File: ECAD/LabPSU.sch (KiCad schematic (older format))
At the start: 45 parts, among them J1 PWR

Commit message: how do i do this
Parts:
- removed U?: LM5118MH, Package_SO:Texas_PWP0020A, symbol Regulator_Switching:LM5118MH
- removed U?: MAX5035EUSA, Package_SO:SOIC-8_3.9x4.9mm_P1.27mm, symbol Regulator_Switching:MAX5035EUSA
- removed U?: INA285, symbol Amplifier_Current:INA285
- added C? (x3): 220uF, symbol Device:CP
- added D? (x2): 1N4148, symbol Device:D
- added R?: 10K, symbol Device:R
- added U? (x3): LM358, symbol Amplifier_Operational:LM358
- added U?: LM5118MH, Package_SO:Texas_PWP0020A, symbol Regulator_Switching:LM5118MH
- added U?: INA285, symbol Amplifier_Current:INA285
- added U?: MAX5035EUSA, Package_SO:SOIC-8_3.9x4.9mm_P1.27mm, symbol Regulator_Switching:MAX5035EUSA
- C? (x2): value C -> 47uF
- C? (x2): value C -> 1uF
- L?: value 300uH -> 470uH
- RV2: value 100K -> 160K
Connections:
- net +10V: now also U?.6 (V+), U?.8 (V+)
- net GND: now also C?.2, C?.2, C?.2, R?.2, U?.13 (CSG), U?.14 (PGND), U?.17 (VCCX), U?.2 (GND), U?.21 (EP), U?.3 (REF2), U?.3 (SGND), U?.4 (V-), U?.6 (AGND), U?.6 (GND), U?.7 (REF1)
- net VBUS: now also U?.1 (VIN), U?.7 (VIN)
- net VOUT: now also U?.1 (-), U?.10 (VOUT)
- net at D?.2 (A), R?.1: now also U?.12 (CS)
- net at Q?.4 (G): now also U?.15 (LO)
- net at C?.1: now also U?.16 (VCC)
- net at C?.1: now also U?.18 (HB)
- net at Q?.4 (G): now also U?.19 (HO)
- net at C?.2, D?.1 (K), L?.1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: now also U?.20 (HS)
- net at R?.1: now also U?.3 (RT)
- net at R?.2: now also U?.4 (EN)
- net at C?.1: now also U?.5 (RAMP)
- net at C?.1: now also U?.7 (SS)
- net FB: now reaches C?.1, R?.2
- net FB: now also D?.1 (K), D?.1 (K), R?.1, U?.2 (-), U?.6 (-), U?.8 (FB)
- net at C?.2, C?.2: now also U?.9 (COMP)
- net at C?.1: now also U?.1 (BST)
- net at C?.1: now also U?.2 (VD)
- net at R?.1, R?.2: now also U?.4 (FB)
- net at R?.1, R?.2: now also U?.5 (ON/~OFF~)
- net at C?.2, D?.1 (K), L?.1: now also U?.8 (LX)
- net at C?.1, C?.1, C?.1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: now also C?.1, C?.1, C?.1, U?.8 (+)
- net at R?.1, RV1.2, RV1.3: now also U?.5 (+)
- net at RV2.1: now also U?.5
- net at R?.1, RV2.2, RV2.3: now also U?.3 (+)
- new net: D?.2 (A), U?.1
- new net: D?.2 (A), U?.7
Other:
- note added: "Rtop/Rbottom = 1000*0.01Ohm*Iout/1.23V - 1\nAdjustable 0.123A to 1A"
- note added: "issue: output cant swing to 100V"
- note removed: "Rtop/Rbottom = 1000*0.01Ohm*Iout/1.23V - 1\nAdjustable 0.123A to 10A"
- moved on the sheet: C?, D?, J1, L?, Q?, R?, RV1A, RV1B, RV2A, RV2B

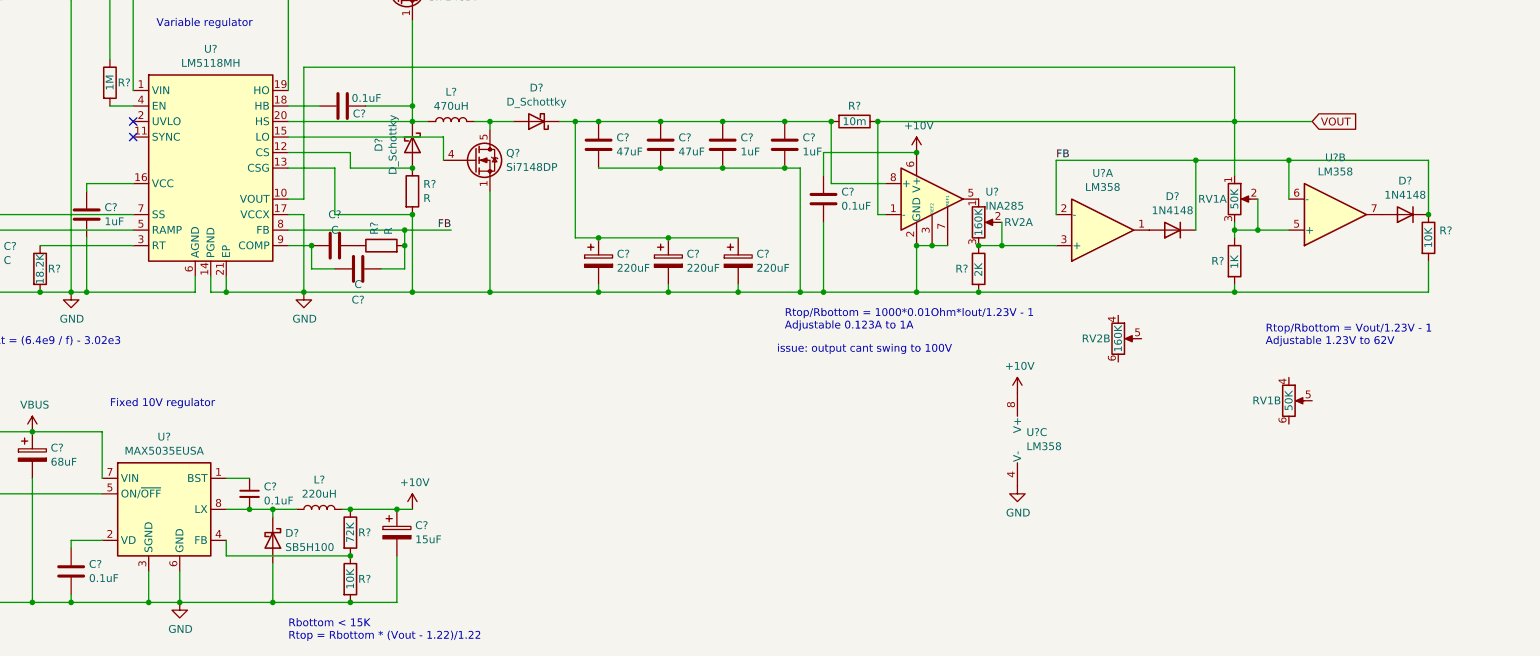
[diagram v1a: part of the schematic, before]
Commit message: vref for current sense
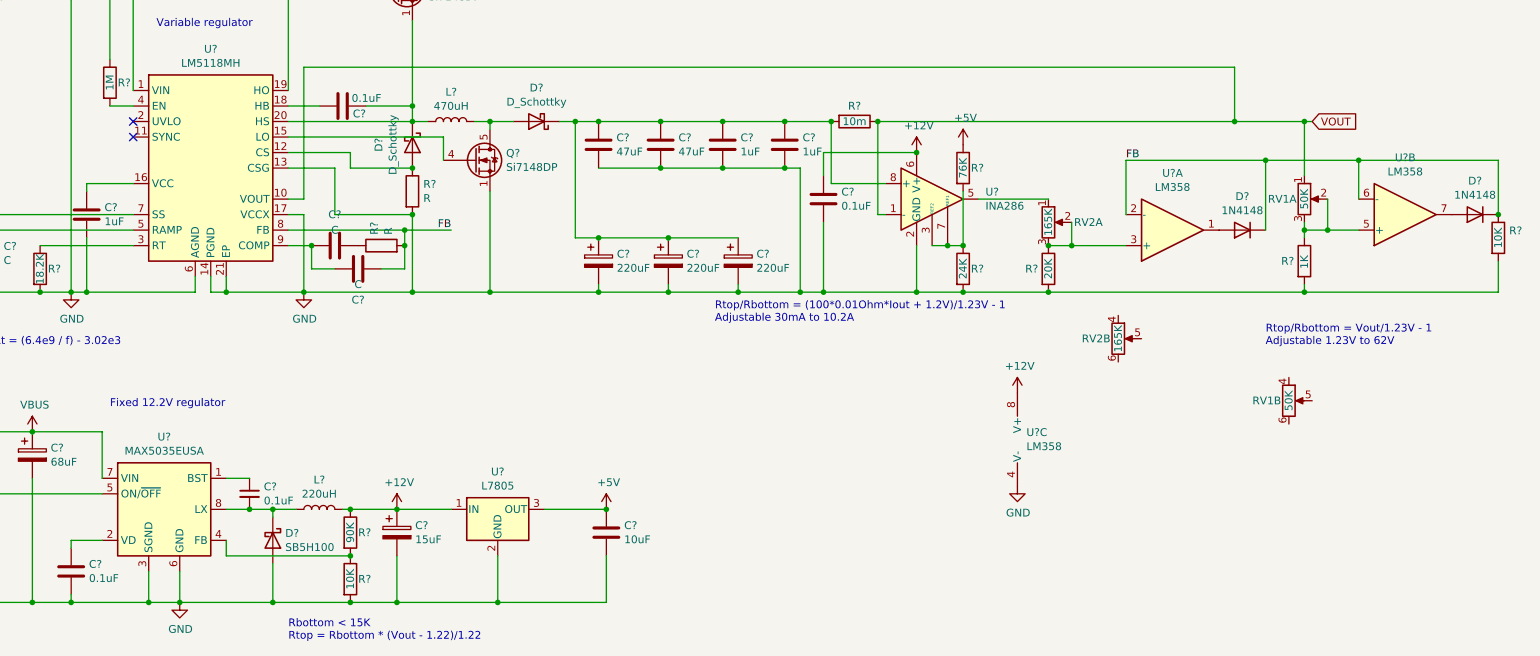
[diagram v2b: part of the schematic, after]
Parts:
- removed U?: INA285, symbol Amplifier_Current:INA285
- added C?: 10uF, symbol Device:C
- added R?: 24K, symbol Device:R
- added R?: 76K, symbol Device:R
- added U?: L7805, symbol Regulator_Linear:L7805
- added U?: INA286, symbol Amplifier_Current:INA286
- R?: value 72K -> 90K
- R?: value 2K -> 20K
- RV2: value 160K -> 165K
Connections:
- net GND: now also C?.2, R?.2, U?.2 (GND), U?.2 (GND)
- net VOUT: now also U?.1 (-)
- net at C?.1, C?.1, C?.1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: now also U?.8 (+)
- net at RV2.1: now also U?.5
- net +10V renamed +12V
- net +12V: now also U?.1 (IN), U?.6 (V+)
- new net: R?.1, R?.2, U?.3 (REF2), U?.7 (REF1)
- new net +5V: C?.1, R?.1, U?.3 (OUT)
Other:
- note added: "Fixed 12.2V regulator"
- note added: "Rtop/Rbottom = (100*0.01Ohm*Iout + 1.2V)/1.23V - 1\nAdjustable 30mA to 10.2A"
- note removed: "Fixed 10V regulator"
- note removed: "Rtop/Rbottom = 1000*0.01Ohm*Iout/1.23V - 1\nAdjustable 0.123A to 1A"
- note removed: "issue: output cant swing to 100V"
- moved on the sheet: D?, R?, RV1A, RV2A, U?A, U?B

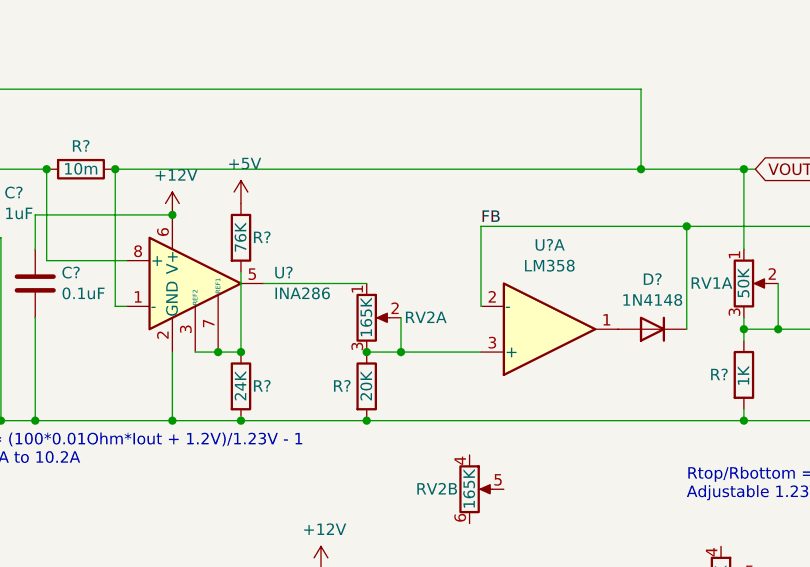
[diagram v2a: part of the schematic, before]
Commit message: add iout label
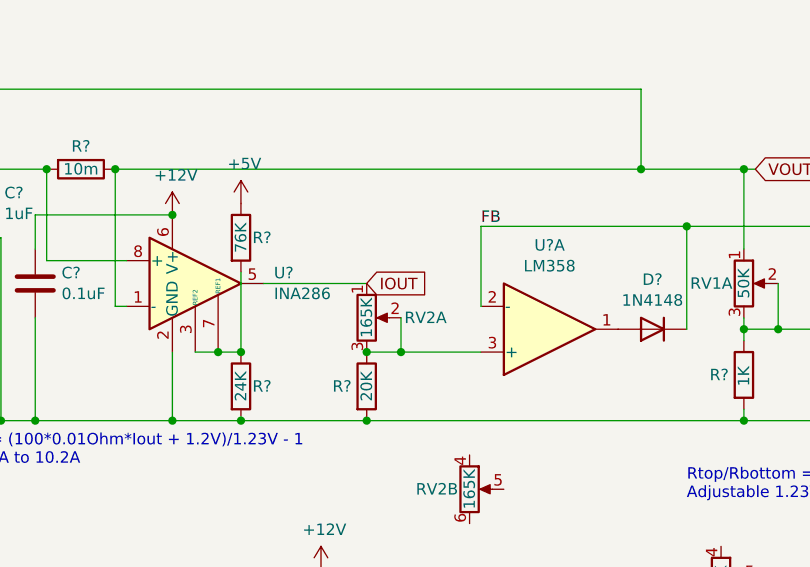
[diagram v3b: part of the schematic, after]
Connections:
- net IOUT: now reaches RV2.1, U?.5
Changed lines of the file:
@@
 $EndComp
 Connection ~ 8500 3000
+Text GLabel 9350 3300 2    50   Input ~ 0
+IOUT
 $EndSCHEMATC

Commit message: add load circuit
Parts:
- added Q?: IRLZ44N, Package_TO_SOT_THT:TO-220-3_Vertical, symbol Transistor_FET:IRLZ44N
- added R? (x10): 10R, symbol Device:R
- added R?: 10m, symbol Device:R
- added R?: 50R, symbol Device:R
- added R?: 1.5K, symbol Device:R
- added RV3: 50K, symbol Device:R_POT_Dual_Separate
- added U2: LM358, symbol Amplifier_Operational:LM358
- added U?: LT6106, Package_TO_SOT_SMD:SOT-23-5, symbol Amplifier_Current:LT6106
- gave numbers to parts that had none: 1
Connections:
- net +12V: now also RV3.1, U2.8 (V+)
- net GND: now also RV3.3, U2.4 (V-), U2.5 (+)
- new net: Q?.1 (G), U2.1
- new net: Q?.3 (S), R?.1, R?.1, R?.1, R?.1, R?.1, R?.1, R?.1, R?.1, R?.1, R?.1, U2.2 (-)
- new net: RV3.2, U2.3 (+)
- new net: U2.6 (-), U2.7
- new net: Q?.2 (D), R?.2, U?.4 (+)
- new net: R?.1, U?.3 (-)
- new net ILOAD: R?.2, U?.1
- new net VLOAD+: R?.1, R?.2, U?.5 (V+)
- new net VLOAD-: R?.1, R?.2, R?.2, R?.2, R?.2, R?.2, R?.2, R?.2, R?.2, R?.2, R?.2, U?.2 (V-)

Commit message: downscale
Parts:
- removed C?: 68uF, symbol Device:CP
- removed C?: 0.1uF, symbol Device:C
- removed C?: 0.1uF, symbol Device:C_Small
- removed C?: 15uF, symbol Device:CP
- removed D?: SB5H100, symbol Device:D_Schottky
- removed L?: 220uH, symbol Device:L
- removed Q?: IRLZ44N, Package_TO_SOT_THT:TO-220-3_Vertical, symbol Transistor_FET:IRLZ44N
- removed R?: 150K, symbol Device:R
- removed R?: 1M, symbol Device:R
- removed R?: 90K, symbol Device:R
- removed R?: 10K, symbol Device:R
- removed R? (x10): 10R, symbol Device:R
- removed R?: 10m, symbol Device:R
- removed R?: 50R, symbol Device:R
- removed R?: 1.5K, symbol Device:R
- removed RV3: 50K, symbol Device:R_POT_Dual_Separate
- removed U2: LM358, symbol Amplifier_Operational:LM358
- removed U?: L7805, symbol Regulator_Linear:L7805
- removed U?: MAX5035EUSA, Package_SO:SOIC-8_3.9x4.9mm_P1.27mm, symbol Regulator_Switching:MAX5035EUSA
- removed U?: LT6106, Package_TO_SOT_SMD:SOT-23-5, symbol Amplifier_Current:LT6106
- added C?: 0.1uF, symbol Device:C
- added C?: 10uF, symbol Device:C
- added D?: D_Schottky, symbol Device:D_Schottky
- added R?: 7.5K, symbol Device:R
- added R?: 1K, symbol Device:R
- added R?: 4m, symbol Device:R
- added U?: INA180A3, Package_TO_SOT_SMD:SOT-23-5, symbol Amplifier_Current:INA138
- added U?: LM1117-5.0, symbol Regulator_Linear:LM1117-5.0
- added U? (x3): LM358, symbol Amplifier_Operational:LM358
- L?: value 470uH -> 330uH
- R?: value 1M -> 100K
- R?: value 10m -> 4m
- R?: value 1K -> 10K
- R?: value 20K -> 100K
- RV1: value 50K -> 400K
- RV2: value 165K -> 300K
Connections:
- net +12V is gone; now on net +5V: C?.1, U1.8 (V+), U?.6 (V+)
- net +5V: now also C?.1, U?.2 (VO), U?.5 (V+)
- net GND: now also C?.2, C?.2, R?.2, U?.1 (GND), U?.2 (GND), U?.4 (V-)
- net VBUS: now also C?.1, R?.2, U?.3 (+), U?.3 (+), U?.3 (VI), U?.8 (V+); no longer C?.1, C?.1, C?.1, C?.1, C?.1, C?.1, Q?.5 (D), R?.1, U?.1 (VIN)
- net at U?.2 (UVLO): now also U?.1
- new net: C?.1, C?.1, C?.1, C?.1, C?.1, C?.1, Q?.5 (D), R?.1, R?.1, U?.1 (VIN), U?.4 (-)
- new net: R?.1, U?.2 (-), U?.7
- new net: R?.1, R?.2, U?.6 (-)
- new net I_IN: U?.1
- new net VSET: U?.5 (+)
- no-connect marks 2 -> 1
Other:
- note added: "Rtop/Rbottom = (100*0.004Ohm*Iout + 1.2V)/1.23V - 1\nAdjustable 75mA to 9.2A"
- note added: "Rtop/Rbottom = Vout/1.23V - 1\nAdjustable 1.23V to 50V"
- note added: "Setpoint control"
- note removed: "Around 14V undervoltage lockout\nUVLO = 1.85V * (Rtop/Rbottom + 1)"
- note removed: "Fixed 12.2V regulator"
- note removed: "Rbottom < 15K\nRtop = Rbottom * (Vout - 1.22)/1.22"
- note removed: "Rtop/Rbottom = (100*0.01Ohm*Iout + 1.2V)/1.23V - 1\nAdjustable 30mA to 10.2A"
- note removed: "Rtop/Rbottom = Vout/1.23V - 1\nAdjustable 1.23V to 62V"
- moved on the sheet: C?, D?, J1, L?, Q?, R?, RV1A, RV1B, RV2A, RV2B, U1A, U1B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

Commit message: Someday I will have to calculate values....
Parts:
- RV1: value 400K -> 300K
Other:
- moved on the sheet: C?, D?, J1, L?, Q?, R?, RV1A, RV1B, RV2A, RV2B, U1A, U1B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

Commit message: diode and rsense selection
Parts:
- C?: value C -> 0.1uF
- D? (x2): value D_Schottky -> V30DM60CL
- R?: value R -> 2.5m
- R?: value 10K -> 9.5K
- R?: value 24K -> 22K
- R?: value 76K -> 78K
- R?: value 7.5K -> 9K
- RV2: value 300K -> 250K
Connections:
- net EN: now reaches R?.2, U?.4 (EN)
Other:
- note added: "Rtop/Rbottom = (100*0.004Ohm*Iout + 1.1V)/1.23V - 1\nAdjustable 325mA to 8A"
- note added: "Rtop/Rbottom = Vout/1.23V - 1\nAdjustable 1.23V to 40V"
- note removed: "Rtop/Rbottom = (100*0.004Ohm*Iout + 1.2V)/1.23V - 1\nAdjustable 75mA to 9.2A"
- note removed: "Rtop/Rbottom = Vout/1.23V - 1\nAdjustable 1.23V to 50V"
- moved on the sheet: C?
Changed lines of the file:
@@
 L Device:C C?
 U 1 1 61BF6F27
-P 3450 3800
-F 0 "C?" H 3565 3846 50  0000 L CNN
-F 1 "C" H 3565 3755 50  0000 L CNN
-F 2 "" H 3488 3650 50  0001 C CNN
-F 3 "~" H 3450 3800 50  0001 C CNN
-	1    3450 3800
+P 3400 3800
+F 0 "C?" H 3515 3846 50  0000 L CNN
+F 1 "0.1uF" H 3515 3755 50  0000 L CNN
+F 2 "" H 3438 3650 50  0001 C CNN
+F 3 "~" H 3400 3800 50  0001 C CNN
+	1    3400 3800
 	1    0    0    -1
 $EndComp
@@
 Cramp = Le-6 / 2Rsense
 Wire Wire Line
-	3450 3950 3450 4050
-Connection ~ 3450 4050
-Wire Wire Line
-	3450 4050 3800 4050
+	3400 3950 3400 4050
 Wire Wire Line
 	3000 3550 4400 3550
 Wire Wire Line
-	3000 4050 3450 4050
+	3000 4050 3400 4050
 $Comp
 L Transistor_FET:Si7336ADP Q?
@@
 Wire Wire Line
 	4800 4050 4800 3950
-Wire Wire Line
-	3450 3650 4400 3650
 $Comp
 L Device:C C?
@@
 U 1 1 61C118EF
 P 7000 2950
-F 0 "D?" H 7000 2733 50  0000 C CNN
-F 1 "D_Schottky" H 7000 2824 50  0000 C CNN
+F 0 "D?" H 7000 2750 50  0000 C CNN
+F 1 "V30DM60CL" H 7000 2850 50  0000 C CNN
 F 2 "" H 7000 2950 50  0001 C CNN
 F 3 "~" H 7000 2950 50  0001 C CNN
@@
 U 1 1 61C12AA1
 P 6200 3100
-F 0 "D?" H 6200 2883 50  0000 C CNN
-F 1 "D_Schottky" H 6200 2974 50  0000 C CNN
+F 0 "D?" V 6150 3000 50  0000 R CNN
+F 1 "V30DM60CL" V 6250 3000 50  0000 R CNN
 F 2 "" H 6200 3100 50  0001 C CNN
 F 3 "~" H 6200 3100 50  0001 C CNN
@@
 P 6200 3400
 F 0 "R?" H 6250 3400 50  0000 L CNN
-F 1 "R" V 6200 3400 50  0000 C CNN
+F 1 "2.5m" V 6200 3400 50  0000 C CNN
 F 2 "" V 6130 3400 50  0001 C CNN
 F 3 "~" H 6200 3400 50  0001 C CNN
@@
 U 1 1 61BFDB17
 P 6600 3200
-F 0 "Q?" H 6804 3246 50  0000 L CNN
-F 1 "Si7148DP" H 6804 3155 50  0000 L CNN
+F 0 "Q?" H 6800 3250 50  0000 L CNN
+F 1 "Si7148DP" H 6800 3150 50  0000 L CNN
 F 2 "Package_SO:PowerPAK_SO-8_Single" H 6800 3125 50  0001 L CIN
 F 3 "https://www.vishay.com/docs/73152/si7336adp.pdf" H 6600 3200 50  0001 L CNN
@@
 P 11950 3850
 F 0 "R?" H 11800 3850 50  0000 L CNN
-F 1 "10K" V 11950 3850 50  0000 C CNN
+F 1 "9.5K" V 11950 3850 50  0000 C CNN
 F 2 "" V 11880 3850 50  0001 C CNN
 F 3 "~" H 11950 3850 50  0001 C CNN
@@
 VOUT
 Text Notes 11500 4250 0    50   ~ 0
-Rtop/Rbottom = Vout/1.23V - 1\nAdjustable 1.23V to 50V
+Rtop/Rbottom = Vout/1.23V - 1\nAdjustable 1.23V to 40V
 Connection ~ 11950 3650
 Wire Wire Line
@@
 P 10750 4350
 F 0 "RV2" H 10700 4350 50  0000 R CNN
-F 1 "300K" V 10750 4350 50  0000 C CNN
+F 1 "250K" V 10750 4350 50  0000 C CNN
 F 2 "" H 10750 4350 50  0001 C CNN
 F 3 "~" H 10750 4350 50  0001 C CNN
@@
 P 10300 3600
 F 0 "RV2" H 10650 3600 50  0000 R CNN
-F 1 "300K" V 10300 3600 50  0000 C CNN
+F 1 "250K" V 10300 3600 50  0000 C CNN
 F 2 "" H 10300 3600 50  0001 C CNN
 F 3 "~" H 10300 3600 50  0001 C CNN
@@
 	1    0    0    -1
 $EndComp
-Text Notes 8150 4250 0    50   ~ 0
-Rtop/Rbottom = (100*0.004Ohm*Iout + 1.2V)/1.23V - 1\nAdjustable 75mA to 9.2A
 Wire Wire Line
 	1700 4800 2050 4800
@@
 	11950 2950 12000 2950
 Connection ~ 10300 3750
-$Comp
-L Device:R R?
-U 1 1 61E35C91
-P 9750 3900
-F 0 "R?" H 9800 3900 50  0000 L CNN
-F 1 "24K" V 9750 3900 50  0000 C CNN
-F 2 "" V 9680 3900 50  0001 C CNN
-F 3 "~" H 9750 3900 50  0001 C CNN
-	1    9750 3900
-	1    0    0    -1
-$EndComp
-$Comp
-L Device:R R?
-U 1 1 61E36C9F
-P 9750 3250
-F 0 "R?" H 9800 3250 50  0000 L CNN
-F 1 "76K" V 9750 3250 50  0000 C CNN
-F 2 "" V 9680 3250 50  0001 C CNN
-F 3 "~" H 9750 3250 50  0001 C CNN
-	1    9750 3250
-	1    0    0    -1
-$EndComp
 Wire Wire Line
 	9850 3450 10300 3450
@@
 P 2200 3400
 F 0 "R?" V 2300 3400 50  0000 C CNN
-F 1 "7.5K" V 2200 3400 50  0000 C CNN
+F 1 "9K" V 2200 3400 50  0000 C CNN
 F 2 "" V 2130 3400 50  0001 C CNN
 F 3 "~" H 2200 3400 50  0001 C CNN
@@
 $EndComp
 Connection ~ 1700 4800
-Text Notes 1850 2650 0    50   ~ 0
+Text Notes 1900 2650 0    50   ~ 0
 Setpoint control
 $Comp
@@
 Text GLabel 2350 2400 2    50   Input ~ 0
 I_IN
+Text Notes 8150 4250 0    50   ~ 0
+Rtop/Rbottom = (100*0.004Ohm*Iout + 1.1V)/1.23V - 1\nAdjustable 325mA to 8A
+$Comp
+L Device:R R?
+U 1 1 61E36C9F
+P 9750 3250
+F 0 "R?" H 9800 3250 50  0000 L CNN
+F 1 "78K" V 9750 3250 50  0000 C CNN
+F 2 "" V 9680 3250 50  0001 C CNN
+F 3 "~" H 9750 3250 50  0001 C CNN
+	1    9750 3250
+	1    0    0    -1
+$EndComp
+$Comp
+L Device:R R?
+U 1 1 61E35C91
+P 9750 3900
+F 0 "R?" H 9800 3900 50  0000 L CNN
+F 1 "22K" V 9750 3900 50  0000 C CNN
+F 2 "" V 9680 3900 50  0001 C CNN
+F 3 "~" H 9750 3900 50  0001 C CNN
+	1    9750 3900
+	1    0    0    -1
+$EndComp
+Wire Wire Line
+	4250 2850 3800 2850
+Connection ~ 4250 2850
+Text GLabel 3800 2850 0    50   Input ~ 0
+EN
+Connection ~ 3400 4050
+Wire Wire Line
+	3400 4050 3800 4050
+Wire Wire Line
+	3400 3650 4400 3650
 $EndSCHEMATC
